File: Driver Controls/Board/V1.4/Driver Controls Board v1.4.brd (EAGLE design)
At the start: 57.5 x 83.8 mm, 22 parts

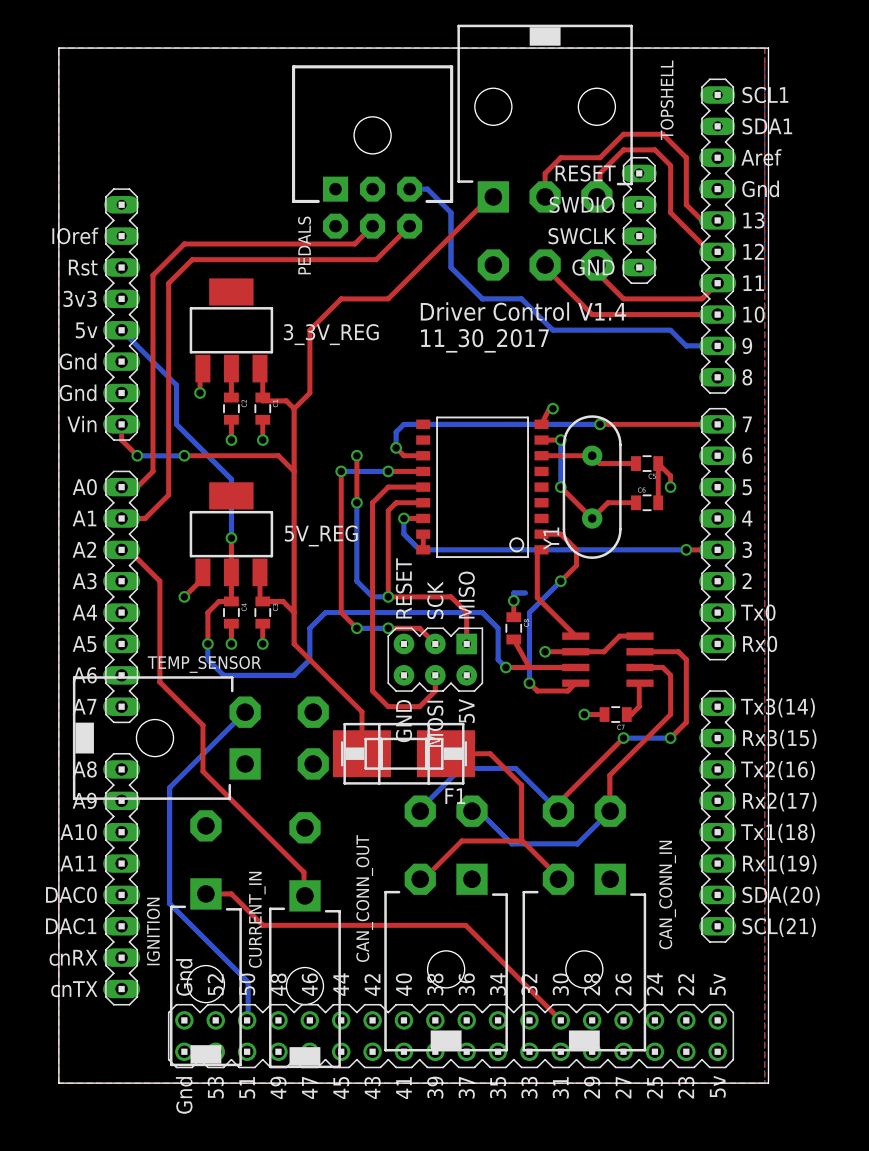
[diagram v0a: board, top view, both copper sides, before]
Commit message: driver control board w/ pulldown resistor
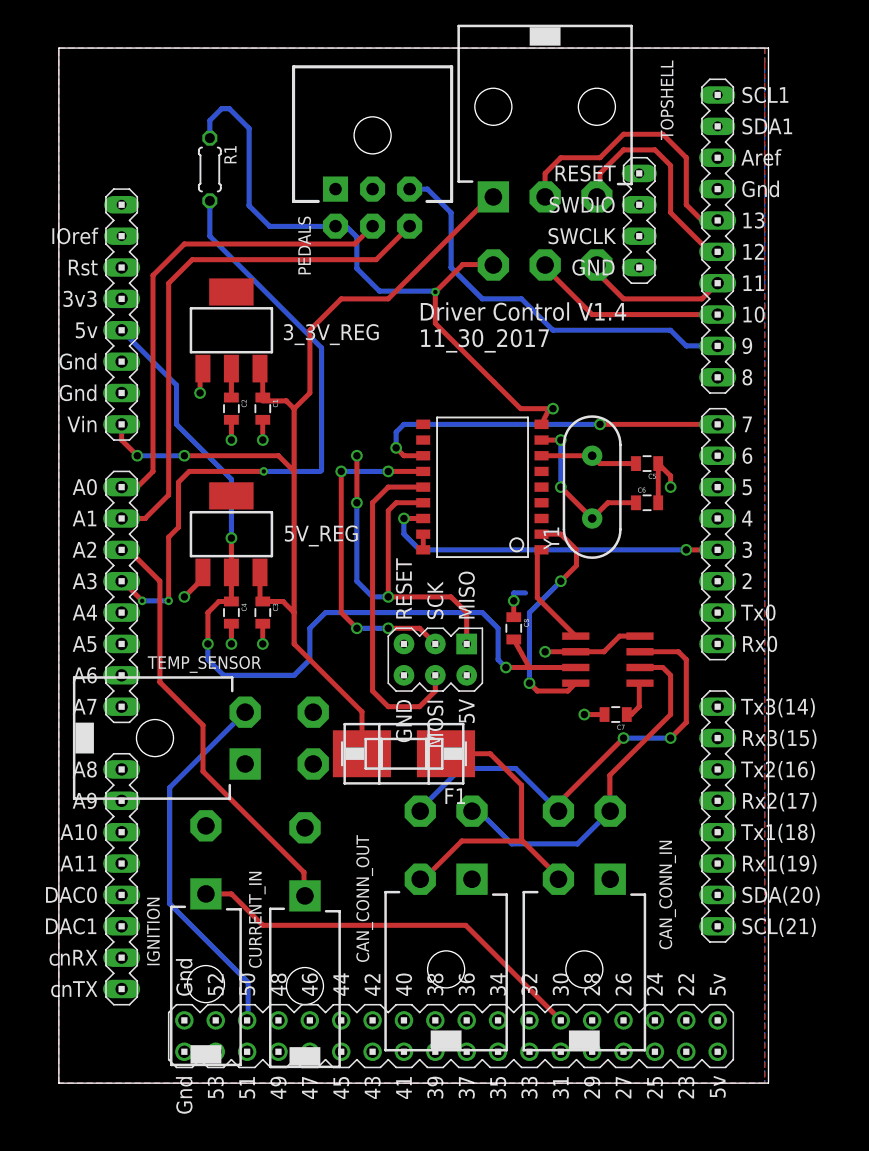
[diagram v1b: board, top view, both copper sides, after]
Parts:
- added R1: (no value), resistor:0204/5
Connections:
- new net N$1: R1.2, U$2.A3
- net GND: now also R1.1
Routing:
- net GND: track 31.2 -> 83.3 mm, vias 11 -> 12
- net N$1: track 0.00 -> 52.0 mm, vias 0 -> 3
